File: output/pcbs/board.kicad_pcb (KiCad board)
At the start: 2 copper layers, 162.1 x 157 mm, 65 parts, among them J1 Jumper, J2 Jumper

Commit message: migrate ergogen 4
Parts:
- added OLED2: OLED, lib:OLED_headers, F.Cu at (119.4, 25.8)
- moved PAD1 9.00 mm to (130.4, 3.89)
- moved PAD2 9.00 mm to (131.2, 0.99)
- moved OLED1 2.50 mm to (105.4, 22.0)
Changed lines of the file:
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@@
   )
         (module lib:OLED_headers (layer F.Cu)
-        (at 107.80475510000001 22.67454 75)
+        (at 105.3899406 22.0274924 75)
         (fp_text reference "OLED1" (at 0 0) (layer F.SilkS) hide (effects (font (size 1.27 1.27) (thickness 0.15))))
         (fp_text value OLED (at 0 -7.3) (layer F.Fab) (effects (font (size 1 1) (thickness 0.15))))
@@
         (net 47 "P1"))
         )
+        (module lib:OLED_headers (layer F.Cu)
+        (at 119.39586510000001 25.780368499999994 255)
+        (fp_text reference "OLED2" (at 0 0) (layer F.SilkS) hide (effects (font (size 1.27 1.27) (thickness 0.15))))
+        (fp_text value OLED (at 0 -7.3) (layer F.Fab) (effects (font (size 1 1) (thickness 0.15))))
+        (pad 4 thru_hole oval (at 1.6 2.18 525) (size 1.7 1.7) (drill 1) (layers *.Cu *.Mask)
+        (net 48 "P0"))
+        (pad 3 thru_hole oval (at 1.6 4.72 525) (size 1.7 1.7) (drill 1) (layers *.Cu *.Mask)
+        (net 49 "P2"))
+        (pad 2 thru_hole oval (at 1.6 7.26 525) (size 1.7 1.7) (drill 1) (layers *.Cu *.Mask)
+        (net 44 "VCC"))
+        (pad 1 thru_hole rect (at 1.6 9.8 525) (size 1.7 1.7) (drill 1) (layers *.Cu *.Mask)
+        (net 42 "GND"))
+        (pad 0 thru_hole oval (at 1.6 12.34 525) (size 1.7 1.7) (drill 1) (layers *.Cu *.Mask)
+        (net 47 "P1"))
+        )
         (module SMDPad (layer F.Cu)
-            (at 121.74381880000001 1.5628724999999992 -15)
+            (at 130.4371513 3.8922438999999986 -15)
             (fp_text reference "PAD1" (at 0 0) (layer F.SilkS) hide (effects (font (size 1.27 1.27) (thickness 0.15))))
             (fp_text value "" (at 0 0) (layer F.SilkS) hide (effects (font (size 1.27 1.27) (thickness 0.15))))
@@
         )
         (module SMDPad (layer F.Cu)
-            (at 122.52027600000001 -1.334905000000001 -15)
+            (at 131.2136084 0.9944663999999985 -15)
             (fp_text reference "PAD2" (at 0 0) (layer F.SilkS) hide (effects (font (size 1.27 1.27) (thickness 0.15))))
             (fp_text value "" (at 0 0) (layer F.SilkS) hide (effects (font (size 1.27 1.27) (thickness 0.15))))

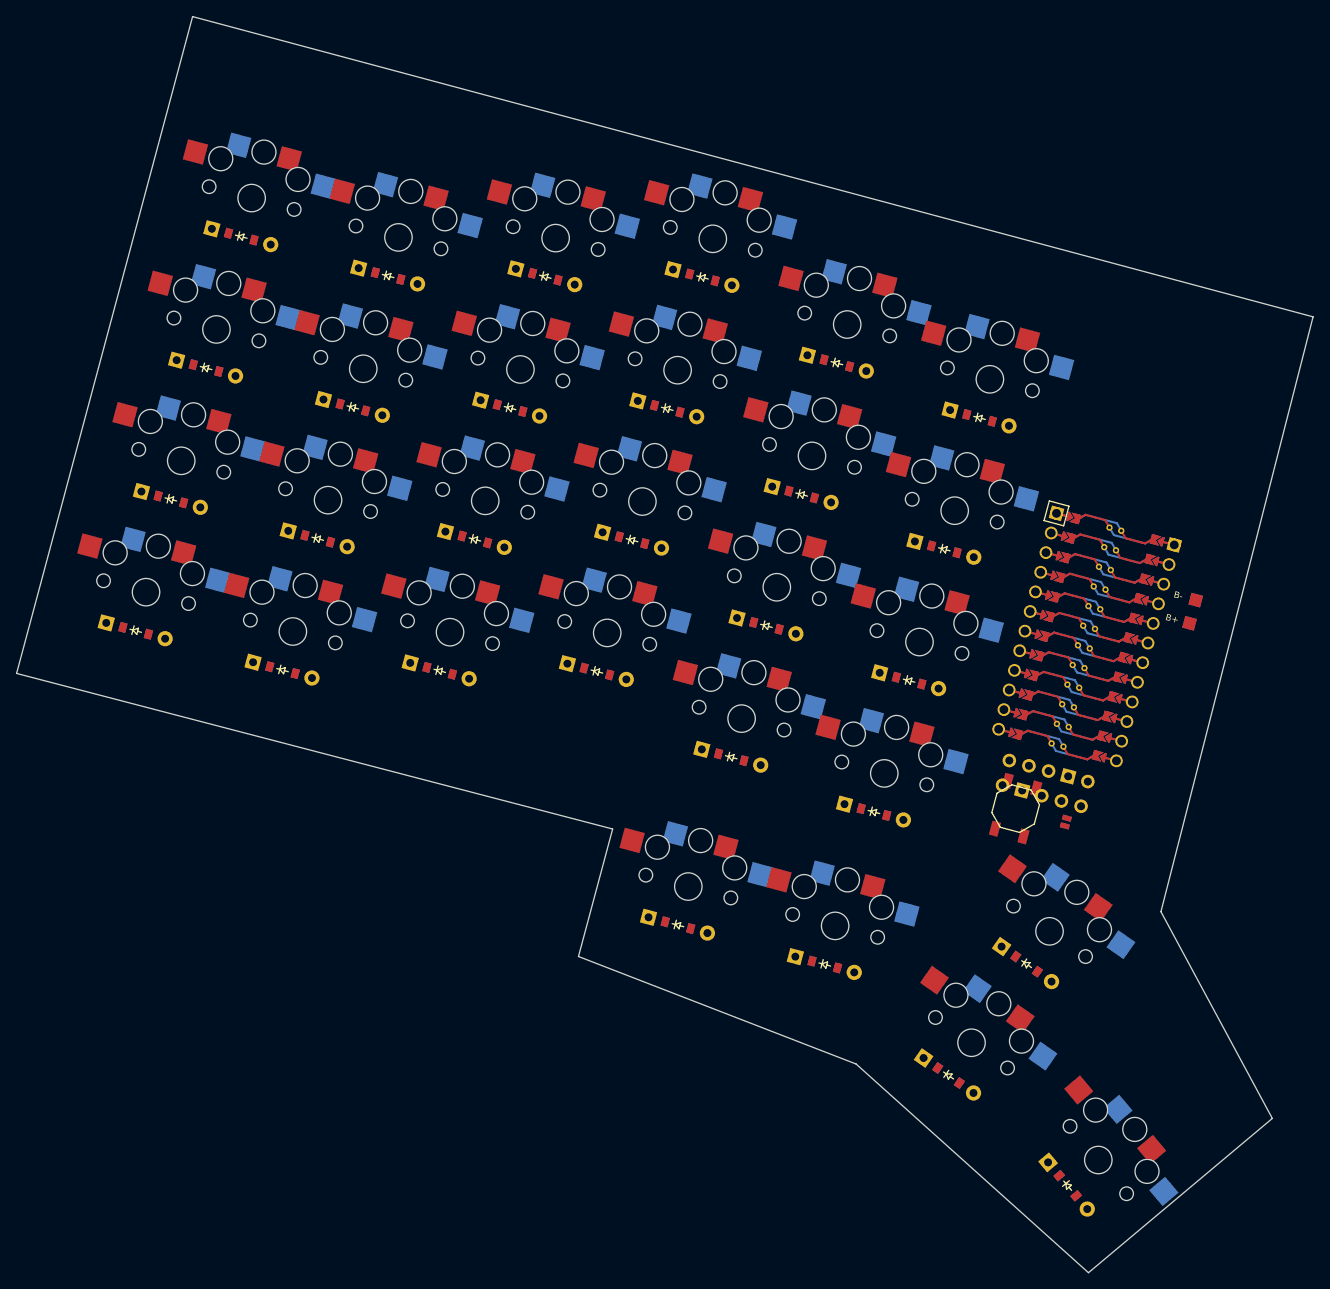
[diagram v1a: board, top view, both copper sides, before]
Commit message: v4 migration complete
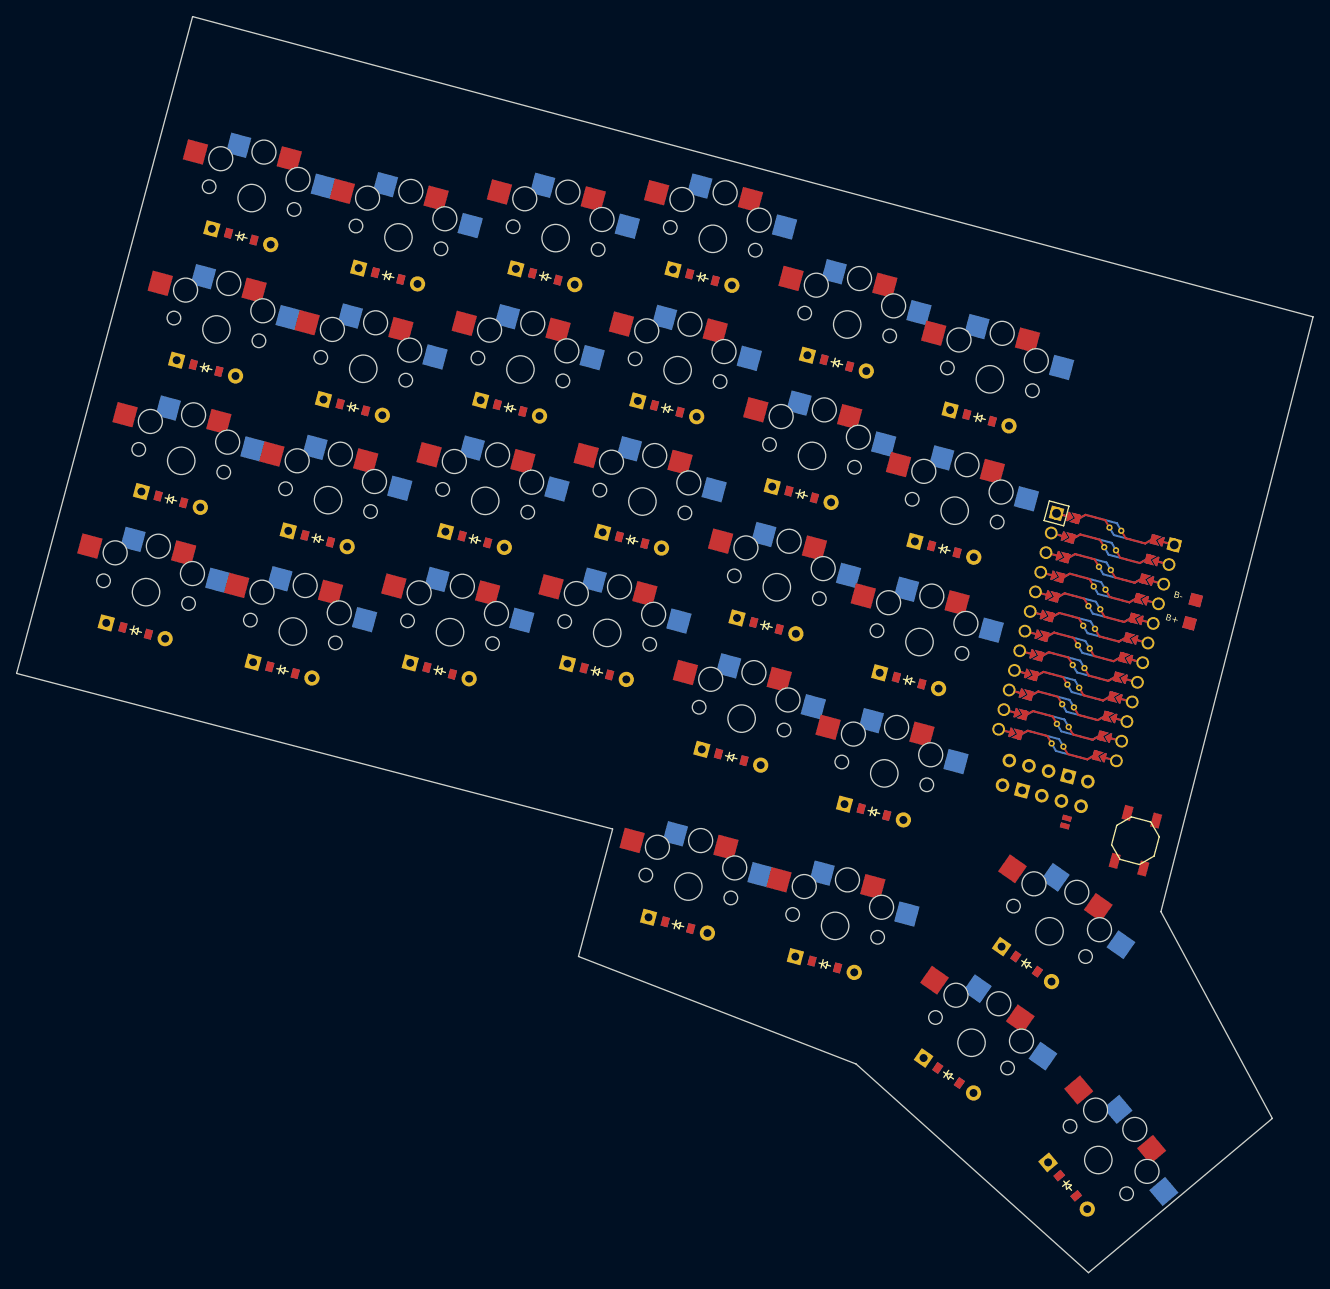
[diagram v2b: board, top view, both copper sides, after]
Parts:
- moved B1 15.5 mm to (123.7, 31.1)
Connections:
- D1 pad 1: outer_bottom -> P7
- D1 pad 2: P7 -> outer_bottom
- D10 pad 1: ring_home -> P6
- D10 pad 2: P6 -> ring_home
- D11 pad 1: ring_top -> P5
- D11 pad 2: P5 -> ring_top
- D12 pad 1: ring_num -> P4
- D12 pad 2: P4 -> ring_num
- D13 pad 1: middle_bottom -> P7
- D13 pad 2: P7 -> middle_bottom
- D14 pad 1: middle_home -> P6
- D14 pad 2: P6 -> middle_home
- D15 pad 1: middle_top -> P5
- D15 pad 2: P5 -> middle_top
- D16 pad 1: middle_num -> P4
- D16 pad 2: P4 -> middle_num
- D17 pad 1: index_bottom -> P7
- D17 pad 2: P7 -> index_bottom
- D18 pad 1: index_home -> P6
- D18 pad 2: P6 -> index_home
- D19 pad 1: index_top -> P5
- D19 pad 2: P5 -> index_top
- D2 pad 1: outer_home -> P6
- D2 pad 2: P6 -> outer_home
- D20 pad 1: index_num -> P4
- D20 pad 2: P4 -> index_num
- D21 pad 1: inner_bottom -> P7
- D21 pad 2: P7 -> inner_bottom
- D22 pad 1: inner_home -> P6
- D22 pad 2: P6 -> inner_home
- D23 pad 1: inner_top -> P5
- D23 pad 2: P5 -> inner_top
- D24 pad 1: inner_num -> P4
- D24 pad 2: P4 -> inner_num
- D25 pad 1: near1_home -> P3
- D25 pad 2: P3 -> near1_home
- D26 pad 1: near2_home -> P3
- D26 pad 2: P3 -> near2_home
- D27 pad 1: home_home -> P3
- D27 pad 2: P3 -> home_home
- D28 pad 1: home_top -> P3
- D28 pad 2: P3 -> home_top
- D29 pad 1: far_home -> P3
- D29 pad 2: P3 -> far_home
- D3 pad 1: outer_top -> P5
- D3 pad 2: P5 -> outer_top
- D4 pad 1: outer_num -> P4
- D4 pad 2: P4 -> outer_num
- D5 pad 1: pinky_bottom -> P7
- D5 pad 2: P7 -> pinky_bottom
- D6 pad 1: pinky_home -> P6
- D6 pad 2: P6 -> pinky_home
- D7 pad 1: pinky_top -> P5
- D7 pad 2: P5 -> pinky_top
- D8 pad 1: pinky_num -> P4
- D8 pad 2: P4 -> pinky_num
- D9 pad 1: ring_bottom -> P7
- D9 pad 2: P7 -> ring_bottom
